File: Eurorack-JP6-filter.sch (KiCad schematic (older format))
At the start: 151 parts, among them J1 JACK_MONO_SW, J2 JACK_MONO_SW, J3 JACK_MONO_SW, J4 JACK_MONO_SW, J5 JACK_MONO_SW, J6 JACK_MONO_SW, P1 CONN_02X05, Q1 BCM857BS, Q2 BCM857BS, Q3 J112, Q4 J112, Q5 J112, Q6 J112, SW1 KS-01Q, U1 TL072-, U10 CD4027, U11 CD40106, U2 TL072-, U3 TL072-, U4 TL072-, U5 LM13700, U6 LM13700, U7 LM13700, U8 DG409, U9 CD4052

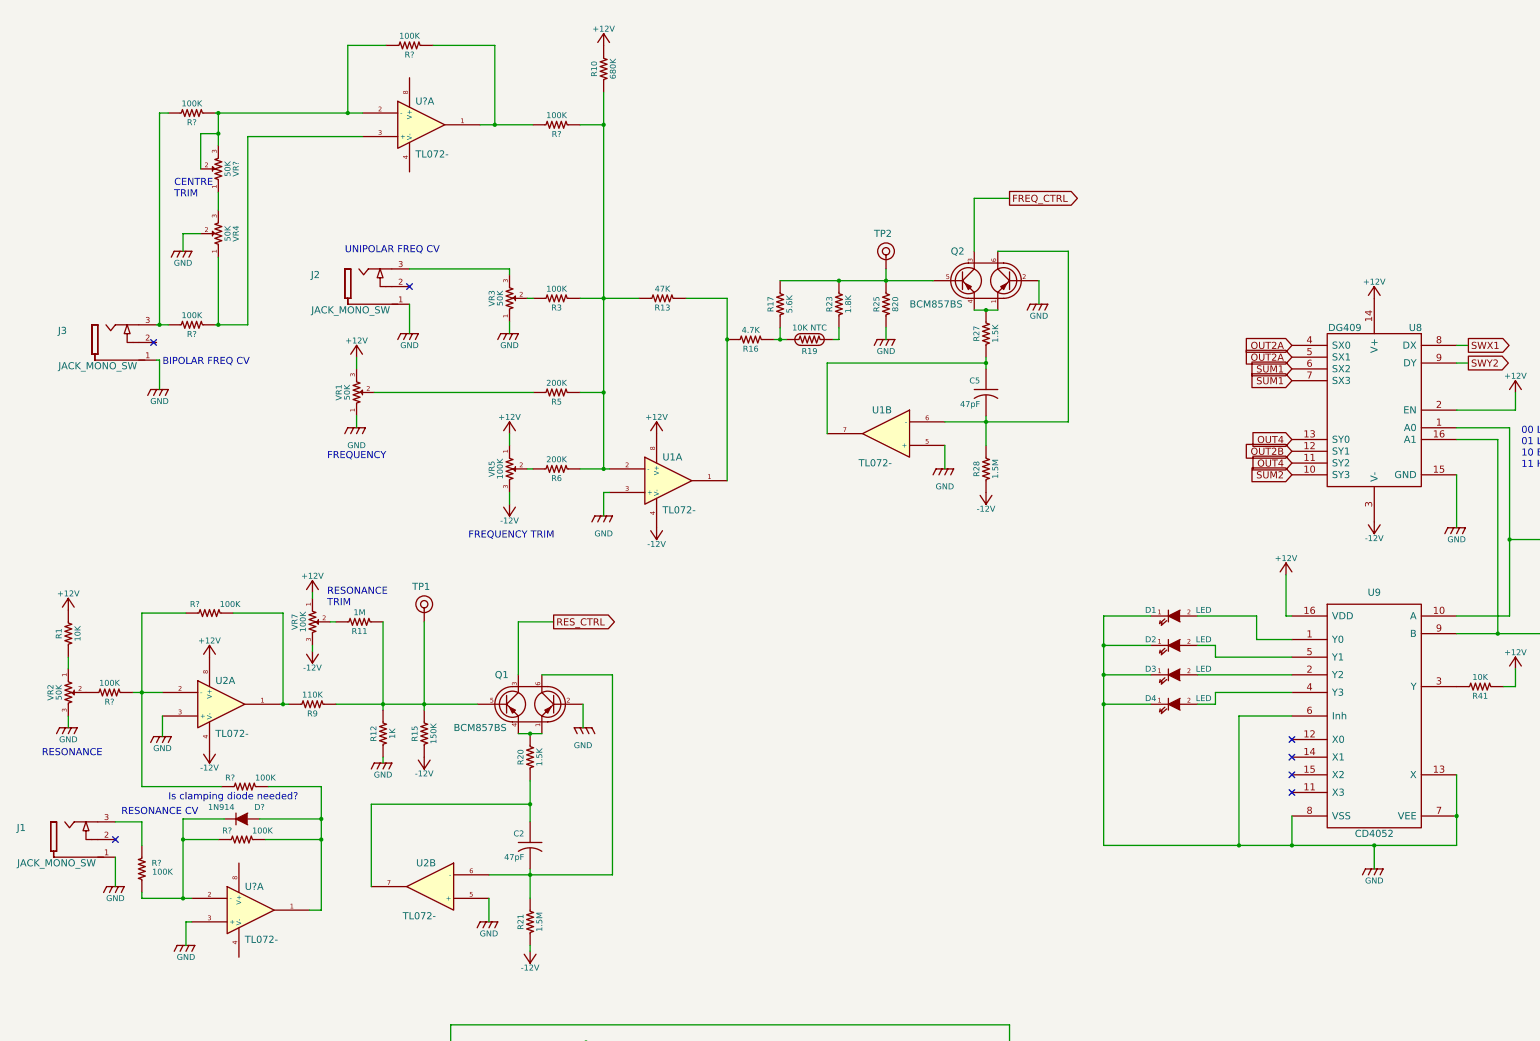
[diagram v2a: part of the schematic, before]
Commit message: replaced op amp servo in exponetial converters with TS321
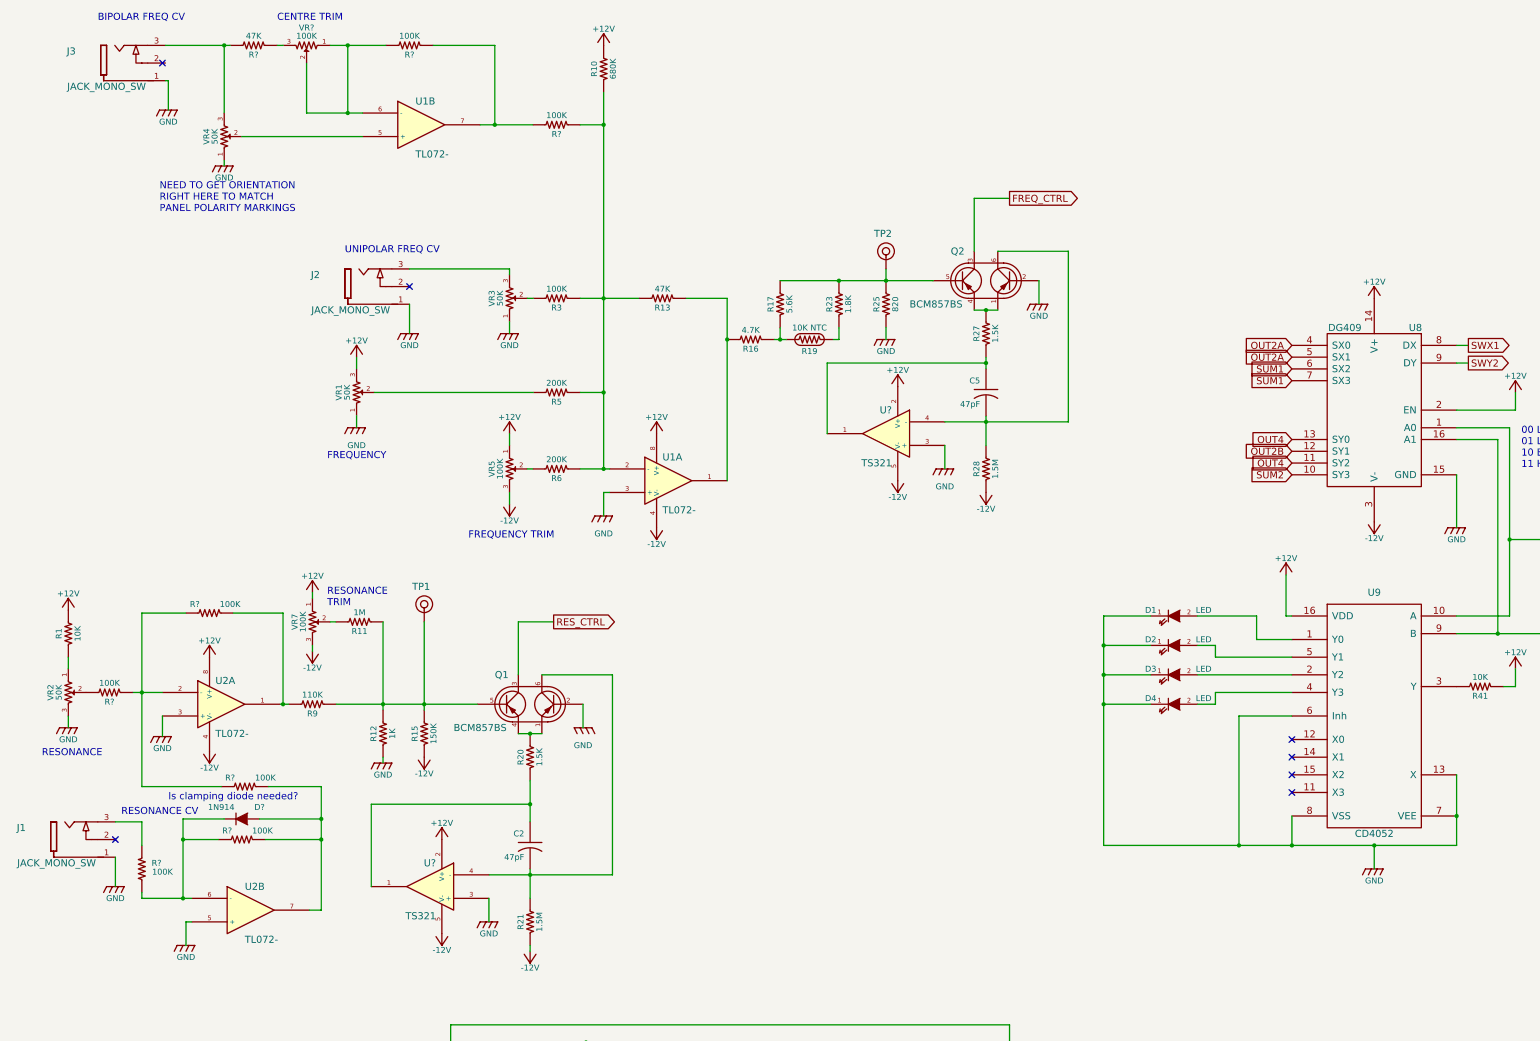
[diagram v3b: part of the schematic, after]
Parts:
- removed R?: 100K, MyModules:SM0603-R-JRL, symbol R_US
- removed unit 2 of U1
- removed unit 2 of U2
- added U? (x2): TS321, symbol TS321
- R?: value 100K -> 47K
- VR?: value 50K -> 100K
- gave numbers to parts that had none: 2
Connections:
- net +12V: now also U?.2 (V+), U?.2 (V+)
- net -12V: now also U?.5 (V-), U?.5 (V-)
- net GND: now also U2.5 (+), VR4.1, U?.3 (+), U?.3 (+); no longer U2.3 (+), VR4.2
- net at C5.2, Q2.6 (C1), R28.1: now also U?.4 (-)
- net at VR4.3: now also J3.3, R?.2; no longer VR?.1
- net at C5.1, R27.2: now also U?.1
- net at C2.2, Q1.6 (C1), R21.1: now also U?.4 (-)
- net at C2.1, R20.2: now also U?.1
- net at R?.1, R?.2: now also U1.7; no longer U1.1
- net at D?.1 (K), R?.1, R?.2: now also U2.6 (-); no longer U2.2 (-)
- net at D?.2 (A), R?.1, R?.1: now also U2.7; no longer U2.1
- new net: U1.5 (+), VR4.2
- new net: R?.2, U1.6 (-), VR?.1, VR?.2
- new net: R?.1, VR?.3
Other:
- note added: "CENTRE TRIM"
- note added: "NEED TO GET ORIENTATION \nRIGHT HERE TO MATCH \nPANEL POLARITY MARKINGS"
- note removed: "CENTRE\nTRIM"
- moved on the sheet: J3, R?, VR4, VR?
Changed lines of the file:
@@
 L POT_US VR4
 U 1 1 553D9840
-P 2250 2600
-F 0 "VR4" H 2250 2450 50  0000 C CNN
-F 1 "50K" H 2250 2520 50  0000 C CNN
-F 2 "MyModules:RV16A-41-JRL" H 2250 2600 60  0001 C CNN
-F 3 "" H 2250 2600 60  0000 C CNN
-	1    2250 2600
-	0    -1   -1   0
+P 2300 1775
+F 0 "VR4" H 2300 1625 50  0000 C CNN
+F 1 "50K" H 2300 1695 50  0000 C CNN
+F 2 "MyModules:RV16A-41-JRL" H 2300 1775 60  0001 C CNN
+F 3 "" H 2300 1775 60  0000 C CNN
+	1    2300 1775
+	0    1    -1   0
 $EndComp
 $Comp
 L JACK_MONO_SW J3
 U 1 1 553D99DC
-P 1475 3525
-F 0 "J3" H 925 3425 60  0000 C CNN
-F 1 "JACK_MONO_SW" H 1225 3725 60  0000 C CNN
-F 2 "MyModules:PJ-301B-JACK" H 1375 3525 60  0001 C CNN
-F 3 "" H 1375 3525 60  0000 C CNN
-	1    1475 3525
+P 1550 1150
+F 0 "J3" H 1000 1050 60  0000 C CNN
+F 1 "JACK_MONO_SW" H 1300 1350 60  0000 C CNN
+F 2 "MyModules:PJ-301B-JACK" H 1450 1150 60  0001 C CNN
+F 3 "" H 1450 1150 60  0000 C CNN
+	1    1550 1150
 	1    0    0    1
 $EndComp
-NoConn ~ 1700 3525
+NoConn ~ 1775 1150
 $Comp
 L GND #PWR08
 U 1 1 553D9B96
-P 1750 3925
-F 0 "#PWR08" H 1750 3675 50  0001 C CNN
-F 1 "GND" H 1750 3825 50  0000 C CNN
-F 2 "" H 1750 3925 60  0000 C CNN
-F 3 "" H 1750 3925 60  0000 C CNN
-	1    1750 3925
+P 1825 1550
+F 0 "#PWR08" H 1825 1300 50  0001 C CNN
+F 1 "GND" H 1825 1450 50  0000 C CNN
+F 2 "" H 1825 1550 60  0000 C CNN
+F 3 "" H 1825 1550 60  0000 C CNN
+	1    1825 1550
 	1    0    0    -1
 $EndComp
@@
 $EndComp
 $Comp
-L TL072- U1
-U 2 1 553DD074
-P 7925 4300
-F 0 "U1" H 7875 4500 60  0000 L CNN
-F 1 "TL072-" H 7875 4050 60  0000 L CNN
-F 2 "MyModules:TSSOP8-JRL" H 7925 4300 60  0001 C CNN
-F 3 "" H 7925 4300 60  0000 C CNN
-	2    7925 4300
-	-1   0    0    -1
-$EndComp
-$Comp
 L GND #PWR013
 U 1 1 553DD52D
@@
 $EndComp
 $Comp
-L TL072- U2
-U 2 1 553E08CC
-P 4050 8150
-F 0 "U2" H 4000 8350 60  0000 L CNN
-F 1 "TL072-" H 4000 7900 60  0000 L CNN
-F 2 "MyModules:TSSOP8-JRL" H 4050 8150 60  0001 C CNN
-F 3 "" H 4050 8150 60  0000 C CNN
-	2    4050 8150
-	-1   0    0    -1
-$EndComp
-$Comp
 L GND #PWR017
 U 1 1 553E08D2
@@
 	9775 7800 12775 7800
 Wire Wire Line
-	12775 7200 12775 7800
+	12775 7800 12775 7200
 Wire Wire Line
 	12075 7800 12075 8000
@@
 $EndComp
 $Comp
-L TL072- U?
-U 1 1 58089E8C
+L TL072- U1
+U 2 1 58089E8C
 P 3975 1675
-F 0 "U?" H 3925 1875 60  0000 L CNN
+F 0 "U1" H 3925 1875 60  0000 L CNN
 F 1 "TL072-" H 3925 1425 60  0000 L CNN
 F 2 "MyModules:TSSOP8-JRL" H 3975 1675 60  0001 C CNN
 F 3 "" H 3975 1675 60  0000 C CNN
-	1    3975 1675
+	2    3975 1675
 	1    0    0    -1
 $EndComp
@@
 	0    1    1    0
 $EndComp
-Wire Wire Line
-	2250 2800 2250 3375
-Wire Wire Line
-	2250 2250 2250 2400
 $Comp
 L R_US R?
@@
 	4475 1675 4925 1675
 Wire Wire Line
-	3675 1000 3350 1000
+	3200 1000 3675 1000
 $Comp
 L GND #PWR?
 U 1 1 58091A16
-P 1950 2750
-F 0 "#PWR?" H 1950 2500 50  0001 C CNN
-F 1 "GND" H 1950 2650 50  0000 C CNN
-F 2 "" H 1950 2750 60  0000 C CNN
-F 3 "" H 1950 2750 60  0000 C CNN
-	1    1950 2750
+P 2300 2025
+F 0 "#PWR?" H 2300 1775 50  0001 C CNN
+F 1 "GND" H 2300 1925 50  0000 C CNN
+F 2 "" H 2300 2025 60  0000 C CNN
+F 3 "" H 2300 2025 60  0000 C CNN
+	1    2300 2025
 	1    0    0    -1
 $EndComp
-Wire Wire Line
-	2100 2600 1950 2600
-Wire Wire Line
-	1950 2600 1950 2750
 Connection ~ 4600 1675
 Wire Wire Line
@@
 L R_US R?
 U 1 1 58097A5F
-P 2025 1575
-F 0 "R?" V 2105 1575 50  0000 C CNN
-F 1 "100K" V 1945 1575 50  0000 C CNN
-F 2 "MyModules:SM0603-R-JRL" H 2025 1575 60  0001 C CNN
-F 3 "" H 2025 1575 60  0000 C CNN
-	1    2025 1575
-	0    1    1    0
-$EndComp
-$Comp
-L R_US R?
-U 1 1 58097C6C
-P 2025 3375
-F 0 "R?" V 2105 3375 50  0000 C CNN
-F 1 "100K" V 1945 3375 50  0000 C CNN
-F 2 "MyModules:SM0603-R-JRL" H 2025 3375 60  0001 C CNN
-F 3 "" H 2025 3375 60  0000 C CNN
-	1    2025 3375
+P 2550 1000
+F 0 "R?" V 2630 1000 50  0000 C CNN
+F 1 "47K" V 2470 1000 50  0000 C CNN
+F 2 "MyModules:SM0603-R-JRL" H 2550 1000 60  0001 C CNN
+F 3 "" H 2550 1000 60  0000 C CNN
+	1    2550 1000
 	0    1    1    0
 $EndComp
 Wire Wire Line
-	2225 3375 2500 3375
-Connection ~ 2250 3375
-Wire Wire Line
-	2250 1750 2100 1750
-Wire Wire Line
-	2100 1750 2100 2050
-Connection ~ 2250 1750
+	1800 1300 1825 1300
 Wire Wire Line
-	1725 3675 1750 3675
-Wire Wire Line
-	1750 3675 1750 3925
-Wire Wire Line
-	1825 1575 1750 1575
-Wire Wire Line
-	1750 1575 1750 3375
-Wire Wire Line
-	1725 3375 1825 3375
-Connection ~ 1750 3375
+	1825 1300 1825 1550
 $Comp
 L R_US R?
@@
 Text Notes 750  7050 0    60   ~ 0
 RESONANCE
-Text Notes 1775 3725 0    60   ~ 0
+Text Notes 1225 800  0    60   ~ 0
 BIPOLAR FREQ CV
 Text Notes 1425 7550 0    60   ~ 0
@@
 Text Notes 3325 2775 0    60   ~ 0
 UNIPOLAR FREQ CV
-Text Notes 1875 2300 0    60   ~ 0
-CENTRE\nTRIM
+Text Notes 2750 800  0    60   ~ 0
+CENTRE TRIM
 $Comp
 L R_US R?
@@
 L POT_US VR?
 U 1 1 5809B3D2
-P 2250 2050
-F 0 "VR?" H 2250 1900 50  0000 C CNN
-F 1 "50K" H 2250 1970 50  0000 C CNN
-F 2 "MyModules:RV16A-41-JRL" H 2250 2050 60  0001 C CNN
-F 3 "" H 2250 2050 60  0000 C CNN
-	1    2250 2050
-	0    -1   -1   0
+P 3000 1000
+F 0 "VR?" H 3000 850 50  0000 C CNN
+F 1 "100K" H 3000 920 50  0000 C CNN
+F 2 "MyModules:RV16A-41-JRL" H 3000 1000 60  0001 C CNN
+F 3 "" H 3000 1000 60  0000 C CNN
+	1    3000 1000
+	-1   0    0    1
 $EndComp
 $Comp
@@
 $EndComp
 $Comp
-L TL072- U?
-U 1 1 580E44DA
+L TL072- U2
+U 2 1 580E44DA
 P 2525 8350
-F 0 "U?" H 2475 8550 60  0000 L CNN
+F 0 "U2" H 2475 8550 60  0000 L CNN
 F 1 "TL072-" H 2475 8100 60  0000 L CNN
 F 2 "MyModules:TSSOP8-JRL" H 2525 8350 60  0001 C CNN
 F 3 "" H 2525 8350 60  0000 C CNN
-	1    2525 8350
+	2    2525 8350
 	1    0    0    -1
 $EndComp
@@
 	1600 5825 1600 7300
 Wire Wire Line
-	2225 1575 3475 1575
-Wire Wire Line
-	3475 1775 2500 1775
-Wire Wire Line
-	2500 1775 2500 3375
-Wire Wire Line
-	2250 1575 2250 1850
-Connection ~ 2250 1575
-Wire Wire Line
 	3350 1000 3350 1575
 Connection ~ 3350 1575
 Text Notes 1825 7425 0    60   ~ 0
 Is clamping diode needed?
+Connection ~ 3350 1000
+Wire Wire Line
+	3000 1150 3000 1575
+Wire Wire Line
+	3000 1575 3475 1575
+Wire Wire Line
+	2750 1000 2800 1000
+Wire Wire Line
+	3475 1775 2450 1775
+Wire Wire Line
+	1800 1000 2350 1000
+Wire Wire Line
+	2300 1000 2300 1575
+Wire Wire Line
+	2300 2025 2300 1975
+Connection ~ 2300 1000
+Text Notes 1750 2425 0    60   ~ 0
+NEED TO GET ORIENTATION \nRIGHT HERE TO MATCH \nPANEL POLARITY MARKINGS
+$Comp
+L TS321 U?
+U 1 1 5812E59A
+P 7925 4300
+F 0 "U?" H 7875 4500 60  0000 L CNN
+F 1 "TS321" H 7875 4050 60  0000 L CNN
+F 2 "" H 7925 4300 60  0000 C CNN
+F 3 "" H 7925 4300 60  0000 C CNN
+	1    7925 4300
+	-1   0    0    -1
+$EndComp
+$Comp
+L +12V #PWR?
+U 1 1 5813028C
+P 8025 3900
+F 0 "#PWR?" H 8025 3750 50  0001 C CNN
+F 1 "+12V" H 8025 4040 50  0000 C CNN
+F 2 "" H 8025 3900 60  0000 C CNN
+F 3 "" H 8025 3900 60  0000 C CNN
+	1    8025 3900
+	1    0    0    -1
+$EndComp
+$Comp
+L -12V #PWR?
+U 1 1 58130480
+P 8025 4700
+F 0 "#PWR?" H 8025 4550 50  0001 C CNN
+F 1 "-12V" H 8025 4840 50  0000 C CNN
+F 2 "" H 8025 4700 60  0000 C CNN
+F 3 "" H 8025 4700 60  0000 C CNN
+	1    8025 4700
+	-1   0    0    1
+$EndComp
+$Comp
+L TS321 U?
+U 1 1 581317C5
+P 4050 8150
+F 0 "U?" H 4000 8350 60  0000 L CNN
+F 1 "TS321" H 4000 7900 60  0000 L CNN
+F 2 "" H 4050 8150 60  0000 C CNN
+F 3 "" H 4050 8150 60  0000 C CNN
+	1    4050 8150
+	-1   0    0    -1
+$EndComp
+$Comp
+L +12V #PWR?
+U 1 1 581317CB
+P 4150 7750
+F 0 "#PWR?" H 4150 7600 50  0001 C CNN
+F 1 "+12V" H 4150 7890 50  0000 C CNN
+F 2 "" H 4150 7750 60  0000 C CNN
+F 3 "" H 4150 7750 60  0000 C CNN
+	1    4150 7750
+	1    0    0    -1
+$EndComp
+$Comp
+L -12V #PWR?
+U 1 1 581317D1
+P 4150 8550
+F 0 "#PWR?" H 4150 8400 50  0001 C CNN
+F 1 "-12V" H 4150 8690 50  0000 C CNN
+F 2 "" H 4150 8550 60  0000 C CNN
+F 3 "" H 4150 8550 60  0000 C CNN
+	1    4150 8550
+	-1   0    0    1
+$EndComp
 $EndSCHEMATC

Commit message: schematic edited, changes simulated. ready to change layout
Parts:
- added C? (x2): 100n, MyModules:SM0603-C-JRL, symbol C_US
- C10: footprint MyModules:2MM-POL-CAP -> Capacitors_SMD:c_elec_5x5.3; Part Number (none) -> UUQ1E100MCL1GB
- C23, C24: footprint MyModules:2MM-POL-CAP -> Capacitors_SMD:c_elec_5x5.3
- U? (x2): footprint (none) -> TO_SOT_Packages_SMD:SOT-23-5
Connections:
- net +12V: now also C?.1
- net -12V: now also C?.2
- net GND: now also C?.1, C?.2
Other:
- moved on the sheet: D6, D?, R?
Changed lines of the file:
@@
 $EndComp
 $Comp
-L CP_US C10
-U 1 1 553D58DE
-P 13700 15200
-F 0 "C10" H 13750 15300 50  0000 L CNN
-F 1 "10μF" H 13750 15100 50  0000 L CNN
-F 2 "MyModules:2MM-POL-CAP" H 13700 15200 60  0001 C CNN
-F 3 "" H 13700 15200 60  0000 C CNN
-	1    13700 15200
-	0    1    1    0
-$EndComp
-$Comp
 L CD4052 U9
 U 1 1 553D5A87
@@
 	1    0    0    1
 $EndComp
-NoConn ~ 1775 1150
 $Comp
 L GND #PWR08
@@
 F 3 "" H 13675 13275 60  0000 C CNN
 	1    13675 13275
-	1    0    0    -1
+	-1   0    0    -1
 $EndComp
 $Comp
@@
 L D D6
 U 1 1 55409A89
-P 14125 12925
-F 0 "D6" H 14125 13025 50  0000 C CNN
-F 1 "1N914" H 14125 12825 50  0000 C CNN
-F 2 "MyModules:SOD323-C1A2" H 14125 12925 60  0001 C CNN
-F 3 "" H 14125 12925 60  0000 C CNN
-	1    14125 12925
+P 14125 12975
+F 0 "D6" H 14125 13075 50  0000 C CNN
+F 1 "1N914" H 14125 12875 50  0000 C CNN
+F 2 "MyModules:SOD323-C1A2" H 14125 12975 60  0001 C CNN
+F 3 "" H 14125 12975 60  0000 C CNN
+	1    14125 12975
 	-1   0    0    1
 $EndComp
@@
 F 0 "C23" H 17800 2000 50  0000 L CNN
 F 1 "10μF" H 17800 1800 50  0000 L CNN
-F 2 "MyModules:2MM-POL-CAP" H 17750 1900 60  0001 C CNN
+F 2 "Capacitors_SMD:c_elec_5x5.3" H 17750 1900 60  0001 C CNN
 F 3 "" H 17750 1900 60  0000 C CNN
 	1    17750 1900
@@
 F 0 "C24" H 17800 2500 50  0000 L CNN
 F 1 "10μF" H 17800 2300 50  0000 L CNN
-F 2 "MyModules:2MM-POL-CAP" H 17750 2400 60  0001 C CNN
+F 2 "Capacitors_SMD:c_elec_5x5.3" H 17750 2400 60  0001 C CNN
 F 3 "" H 17750 2400 60  0000 C CNN
 	1    17750 2400
@@
 Wire Wire Line
 	14275 12675 14275 13125
-Connection ~ 14275 12925
+Connection ~ 14275 12975
 Wire Wire Line
 	13675 12025 13675 13075
 Wire Wire Line
 	13975 12675 13975 13125
-Connection ~ 13975 12925
+Connection ~ 13975 12975
 Wire Wire Line
 	13675 13475 13675 13525
@@
 Wire Wire Line
 	1800 1300 1825 1300
-Wire Wire Line
-	1825 1300 1825 1550
 $Comp
 L R_US R?
@@
 Text Notes 1225 800  0    60   ~ 0
 BIPOLAR FREQ CV
-Text Notes 1425 7550 0    60   ~ 0
+Text Notes 625  8100 0    60   ~ 0
 RESONANCE CV
 Text Notes 3175 5775 0    60   ~ 0
@@
 L D D?
 U 1 1 580D0873
-P 2450 7575
-F 0 "D?" H 2600 7675 50  0000 C CNN
-F 1 "1N914" H 2275 7675 50  0000 C CNN
-F 2 "MyModules:SOD323-C1A2" H 2450 7575 60  0001 C CNN
-F 3 "" H 2450 7575 60  0000 C CNN
-	1    2450 7575
+P 2450 7725
+F 0 "D?" H 2600 7825 50  0000 C CNN
+F 1 "1N914" H 2275 7825 50  0000 C CNN
+F 2 "MyModules:SOD323-C1A2" H 2450 7725 60  0001 C CNN
+F 3 "" H 2450 7725 60  0000 C CNN
+	1    2450 7725
 	1    0    0    -1
 $EndComp
@@
 L R_US R?
 U 1 1 580E55D6
-P 2450 7750
-F 0 "R?" V 2375 7625 50  0000 C CNN
-F 1 "100K" V 2375 7925 50  0000 C CNN
-F 2 "MyModules:SM0603-R-JRL" H 2450 7750 60  0001 C CNN
-F 3 "" H 2450 7750 60  0000 C CNN
-	1    2450 7750
+P 2450 7900
+F 0 "R?" V 2375 7775 50  0000 C CNN
+F 1 "100K" V 2375 8075 50  0000 C CNN
+F 2 "MyModules:SM0603-R-JRL" H 2450 7900 60  0001 C CNN
+F 3 "" H 2450 7900 60  0000 C CNN
+	1    2450 7900
 	0    1    1    0
 $EndComp
 Wire Wire Line
-	2250 7750 1950 7750
+	2250 7900 1950 7900
 Wire Wire Line
-	1950 7575 1950 8250
+	1950 7725 1950 8250
 Wire Wire Line
 	1600 8250 2025 8250
 Wire Wire Line
-	3125 7750 2650 7750
+	3125 7900 2650 7900
 Wire Wire Line
 	3125 7300 3125 8350
@@
 Wire Wire Line
 	2675 7300 3125 7300
-Connection ~ 3125 7750
+Connection ~ 3125 7900
 Wire Wire Line
-	2600 7575 3125 7575
-Connection ~ 3125 7575
+	2600 7725 3125 7725
+Connection ~ 3125 7725
 Wire Wire Line
-	2300 7575 1950 7575
-Connection ~ 1950 7750
+	2300 7725 1950 7725
+Connection ~ 1950 7900
 Wire Wire Line
 	1600 7300 2275 7300
@@
 	3350 1000 3350 1575
 Connection ~ 3350 1575
-Text Notes 1825 7425 0    60   ~ 0
+Text Notes 1850 7525 0    60   ~ 0
 Is clamping diode needed?
 Connection ~ 3350 1000
@@
 F 0 "U?" H 7875 4500 60  0000 L CNN
 F 1 "TS321" H 7875 4050 60  0000 L CNN
-F 2 "" H 7925 4300 60  0000 C CNN
+F 2 "TO_SOT_Packages_SMD:SOT-23-5" H 7925 4300 60  0001 C CNN
 F 3 "" H 7925 4300 60  0000 C CNN
 	1    7925 4300
@@
 F 0 "U?" H 4000 8350 60  0000 L CNN
 F 1 "TS321" H 4000 7900 60  0000 L CNN
-F 2 "" H 4050 8150 60  0000 C CNN
+F 2 "TO_SOT_Packages_SMD:SOT-23-5" H 4050 8150 60  0001 C CNN
 F 3 "" H 4050 8150 60  0000 C CNN
 	1    4050 8150
@@
 	-1   0    0    1
 $EndComp
+Wire Wire Line
+	1825 1300 1825 1550
+NoConn ~ 1800 1150
+$Comp
+L C_US C?
+U 1 1 5814908E
+P 17375 1900
+F 0 "C?" H 17425 2000 50  0000 L CNN
+F 1 "100n" H 17425 1800 50  0000 L CNN
+F 2 "MyModules:SM0603-C-JRL" H 17375 1900 60  0001 C CNN
+F 3 "" H 17375 1900 60  0000 C CNN
+	1    17375 1900
+	1    0    0    -1
+$EndComp
+$Comp
+L C_US C?
+U 1 1 5814929C
+P 17375 2400
+F 0 "C?" H 17425 2500 50  0000 L CNN
+F 1 "100n" H 17425 2300 50  0000 L CNN
+F 2 "MyModules:SM0603-C-JRL" H 17375 2400 60  0001 C CNN
+F 3 "" H 17375 2400 60  0000 C CNN
+	1    17375 2400
+	1    0    0    -1
+$EndComp
+Connection ~ 17375 1700
+Connection ~ 17375 2600
+Wire Wire Line
+	17375 2100 17375 2200
+Connection ~ 17375 2150
+$Comp
+L CP_US C10
+U 1 1 553D58DE
+P 13700 15200
+F 0 "C10" V 13525 15000 50  0000 L CNN
+F 1 "10μF" V 13525 15225 50  0000 L CNN
+F 2 "Capacitors_SMD:c_elec_5x5.3" H 13700 15200 60  0001 C CNN
+F 3 "" H 13700 15200 60  0000 C CNN
+F 4 "UUQ1E100MCL1GB" V 13875 15200 60  0000 C CNN "Part Number"
+	1    13700 15200
+	0    1    1    0
+$EndComp
 $EndSCHEMATC

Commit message: annoated additional components and passed ERC
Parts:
- gave numbers to parts that had none: 14

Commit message: hacking together v1.3 pcb
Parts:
- VR5, VR7: footprint MyModules:Bourns_3362P -> MyModules:TC33X-2
- VR8: footprint MyModules:RV16A-41-JRL -> MyModules:TC33X-2
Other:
- note added: "NEED TO GET VR4\nORIENTATION RIGHT\nHERE TO MATCH PANEL\nPOLARITY MARKINGS"
- note removed: "NEED TO GET ORIENTATION \nRIGHT HERE TO MATCH \nPANEL POLARITY MARKINGS"
- moved on the sheet: C2, C5, D10, J1, J2, J3, Q1, Q2, R1, R10, R11, R12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
